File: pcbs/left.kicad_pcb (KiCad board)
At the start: 2 copper layers, 123.1 x 93.2 mm, 27 parts

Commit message: Remove top two mounting holes
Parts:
- removed H4, H5: , ceoloide:mounting_hole_plated
- moved H3 104.9 mm to (198.6, 101.6), turned to -26 degrees
- moved H1 68.4 mm to (94.4, 113.7)
- moved H2 67.2 mm to (135.1, 91.7)
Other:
- outline, holes or cut-outs redrawn
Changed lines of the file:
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@@
   (footprint "ceoloide:mounting_hole_plated"
     (layer "F.Cu")
-    (at 94.25093449999999 45.301295800000005 6)
+    (at 94.3972168 113.6604839 6)
     (property "Reference" "H1"
       (at 0 3 6)
@@
   (footprint "ceoloide:mounting_hole_plated"
     (layer "F.Cu")
-    (at 181.1483666 42.684291099999996 0)
+    (at 135.1483667 91.68429119999999 0)
     (property "Reference" "H2"
       (at 0 3 0)
@@
   (footprint "ceoloide:mounting_hole_plated"
     (layer "F.Cu")
-    (at 94.3972168 113.6604839 6)
+    (at 198.6292952 101.55924569999999 -26)
     (property "Reference" "H3"
-      (at 0 3 6)
-      (layer "F.SilkS")
-      hide
-      (effects (font (size 1 1) (thickness 0.15)))
-    )
-    (pad "" thru_hole circle (at 0 0 6) (size 3.8000000000000003 3.8000000000000003) (drill 2.2) (layers "*.Cu" "*.Mask"))
-    (fp_circle (center 0 0) (end -2.1500000000000004 0) (layer "F.CrtYd") (stroke (width 0.05) (type solid)) (fill none))
-    (fp_circle (center 0 0) (end -2.1500000000000004 0) (layer "B.CrtYd") (stroke (width 0.05) (type solid)) (fill none))
-  )
-  (footprint "ceoloide:mounting_hole_plated"
-    (layer "F.Cu")
-    (at 135.1483667 91.68429119999999 0)
-    (property "Reference" "H4"
-      (at 0 3 0)
-      (layer "F.SilkS")
-      hide
-      (effects (font (size 1 1) (thickness 0.15)))
-    )
-    (pad "" thru_hole circle (at 0 0 0) (size 3.8000000000000003 3.8000000000000003) (drill 2.2) (layers "*.Cu" "*.Mask"))
-    (fp_circle (center 0 0) (end -2.1500000000000004 0) (layer "F.CrtYd") (stroke (width 0.05) (type solid)) (fill none))
-    (fp_circle (center 0 0) (end -2.1500000000000004 0) (layer "B.CrtYd") (stroke (width 0.05) (type solid)) (fill none))
-  )
-  (footprint "ceoloide:mounting_hole_plated"
-    (layer "F.Cu")
-    (at 198.6292952 101.55924569999999 -26)
-    (property "Reference" "H5"
       (at 0 3 -26)
       (layer "F.SilkS")
@@
 (gr_line (start 143.1483666 95.68429119999999) (end 113.1483666 95.68429119999999) (layer Edge.Cuts) (stroke (width 0.15) (type default)))
 (gr_arc (start 113.1483666 95.68429119999999) (mid 112.4412598 95.97718439999998) (end 112.1483666 96.68429119999999) (layer Edge.Cuts) (stroke (width 0.15) (type default)))
-(gr_circle (center 94.25093449999999 45.301295800000005) (end 96.05093449999998 45.301295800000005) (layer Edge.Cuts) (stroke (width 0.15) (type default)) (fill none))
-(gr_circle (center 181.1483666 42.684291099999996) (end 182.9483666 42.684291099999996) (layer Edge.Cuts) (stroke (width 0.15) (type default)) (fill none))
 (gr_circle (center 135.1483667 91.68429119999999) (end 136.9483667 91.68429119999999) (layer Edge.Cuts) (stroke (width 0.15) (type default)) (fill none))
 (gr_circle (center 198.6292952 101.55924569999999) (end 200.4292952 101.55924569999999) (layer Edge.Cuts) (stroke (width 0.15) (type default)) (fill none))

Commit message: Remove bottom middle hole
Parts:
- removed H3: , ceoloide:mounting_hole_plated
- moved H2 64.2 mm to (198.6, 101.6), turned to -26 degrees
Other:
- outline, holes or cut-outs redrawn
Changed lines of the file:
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@@
-  (footprint "ceoloide:mounting_hole_plated"
-    (layer "F.Cu")
-    (at 135.1483667 91.68429119999999 0)
-    (property "Reference" "H2"
-      (at 0 3 0)
-      (layer "F.SilkS")
-      hide
-      (effects (font (size 1 1) (thickness 0.15)))
-    )
-    (pad "" thru_hole circle (at 0 0 0) (size 3.8000000000000003 3.8000000000000003) (drill 2.2) (layers "*.Cu" "*.Mask"))
-    (fp_circle (center 0 0) (end -2.1500000000000004 0) (layer "F.CrtYd") (stroke (width 0.05) (type solid)) (fill none))
-    (fp_circle (center 0 0) (end -2.1500000000000004 0) (layer "B.CrtYd") (stroke (width 0.05) (type solid)) (fill none))
-  )
   (footprint "ceoloide:mounting_hole_plated"
     (layer "F.Cu")
     (at 198.6292952 101.55924569999999 -26)
-    (property "Reference" "H3"
+    (property "Reference" "H2"
       (at 0 3 -26)
       (layer "F.SilkS")
@@
 (gr_line (start 143.1483666 95.68429119999999) (end 113.1483666 95.68429119999999) (layer Edge.Cuts) (stroke (width 0.15) (type default)))
 (gr_arc (start 113.1483666 95.68429119999999) (mid 112.4412598 95.97718439999998) (end 112.1483666 96.68429119999999) (layer Edge.Cuts) (stroke (width 0.15) (type default)))
-(gr_circle (center 135.1483667 91.68429119999999) (end 136.9483667 91.68429119999999) (layer Edge.Cuts) (stroke (width 0.15) (type default)) (fill none))
 (gr_circle (center 198.6292952 101.55924569999999) (end 200.4292952 101.55924569999999) (layer Edge.Cuts) (stroke (width 0.15) (type default)) (fill none))
 (gr_circle (center 94.3972168 113.6604839) (end 96.19721679999999 113.6604839) (layer Edge.Cuts) (stroke (width 0.15) (type default)) (fill none))

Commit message: Remove bottom right hole
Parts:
- removed H2: , ceoloide:mounting_hole_plated
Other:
- outline, holes or cut-outs redrawn
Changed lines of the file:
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@@
-    (fp_circle (center 0 0) (end -2.1500000000000004 0) (layer "B.CrtYd") (stroke (width 0.05) (type solid)) (fill none))
-  )
-  (footprint "ceoloide:mounting_hole_plated"
-    (layer "F.Cu")
-    (at 198.6292952 101.55924569999999 -26)
-    (property "Reference" "H2"
-      (at 0 3 -26)
-      (layer "F.SilkS")
-      hide
-      (effects (font (size 1 1) (thickness 0.15)))
-    )
-    (pad "" thru_hole circle (at 0 0 -26) (size 3.8000000000000003 3.8000000000000003) (drill 2.2) (layers "*.Cu" "*.Mask"))
-    (fp_circle (center 0 0) (end -2.1500000000000004 0) (layer "F.CrtYd") (stroke (width 0.05) (type solid)) (fill none))
     (fp_circle (center 0 0) (end -2.1500000000000004 0) (layer "B.CrtYd") (stroke (width 0.05) (type solid)) (fill none))
   )
@@
 (gr_line (start 143.1483666 95.68429119999999) (end 113.1483666 95.68429119999999) (layer Edge.Cuts) (stroke (width 0.15) (type default)))
 (gr_arc (start 113.1483666 95.68429119999999) (mid 112.4412598 95.97718439999998) (end 112.1483666 96.68429119999999) (layer Edge.Cuts) (stroke (width 0.15) (type default)))
-(gr_circle (center 198.6292952 101.55924569999999) (end 200.4292952 101.55924569999999) (layer Edge.Cuts) (stroke (width 0.15) (type default)) (fill none))
 (gr_circle (center 94.3972168 113.6604839) (end 96.19721679999999 113.6604839) (layer Edge.Cuts) (stroke (width 0.15) (type default)) (fill none))
 (gr_line (start 112.1483666 96.68429119999999) (end 112.1483666 116.68429119999999) (layer F.SilkS) (stroke (width 0.15) (type default)))

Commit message: Remove bottom left hole
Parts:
- removed H1: , ceoloide:mounting_hole_plated
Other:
- outline, holes or cut-outs redrawn
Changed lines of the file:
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@@
     )
-  )
-  (footprint "ceoloide:mounting_hole_plated"
-    (layer "F.Cu")
-    (at 94.3972168 113.6604839 6)
-    (property "Reference" "H1"
-      (at 0 3 6)
-      (layer "F.SilkS")
-      hide
-      (effects (font (size 1 1) (thickness 0.15)))
-    )
-    (pad "" thru_hole circle (at 0 0 6) (size 3.8000000000000003 3.8000000000000003) (drill 2.2) (layers "*.Cu" "*.Mask"))
-    (fp_circle (center 0 0) (end -2.1500000000000004 0) (layer "F.CrtYd") (stroke (width 0.05) (type solid)) (fill none))
-    (fp_circle (center 0 0) (end -2.1500000000000004 0) (layer "B.CrtYd") (stroke (width 0.05) (type solid)) (fill none))
   )
   (zone
@@
 (gr_line (start 143.1483666 95.68429119999999) (end 113.1483666 95.68429119999999) (layer Edge.Cuts) (stroke (width 0.15) (type default)))
 (gr_arc (start 113.1483666 95.68429119999999) (mid 112.4412598 95.97718439999998) (end 112.1483666 96.68429119999999) (layer Edge.Cuts) (stroke (width 0.15) (type default)))
-(gr_circle (center 94.3972168 113.6604839) (end 96.19721679999999 113.6604839) (layer Edge.Cuts) (stroke (width 0.15) (type default)) (fill none))
 (gr_line (start 112.1483666 96.68429119999999) (end 112.1483666 116.68429119999999) (layer F.SilkS) (stroke (width 0.15) (type default)))
 (gr_arc (start 112.1483666 116.68429119999999) (mid 112.4412598 117.391398) (end 113.1483666 117.68429119999999) (layer F.SilkS) (stroke (width 0.15) (type default)))

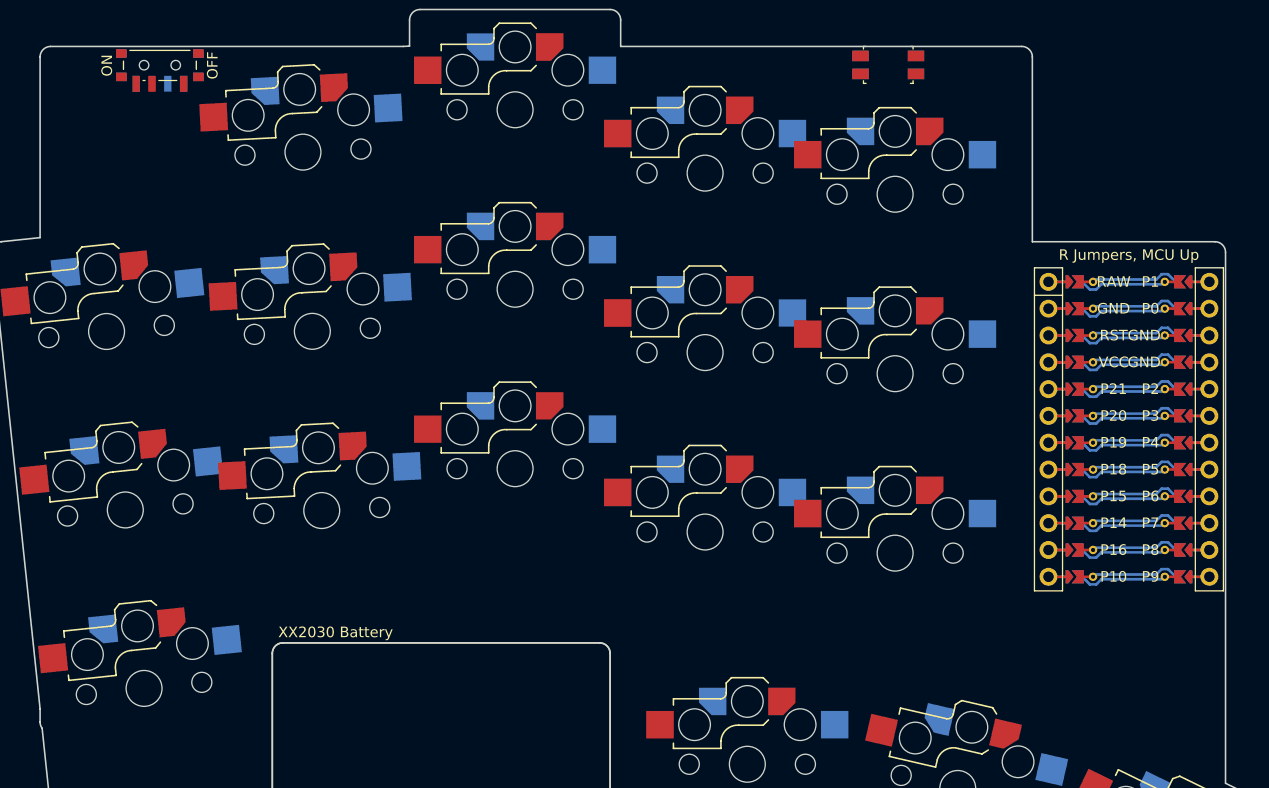
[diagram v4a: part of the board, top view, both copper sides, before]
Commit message: Restore holes except bottom left
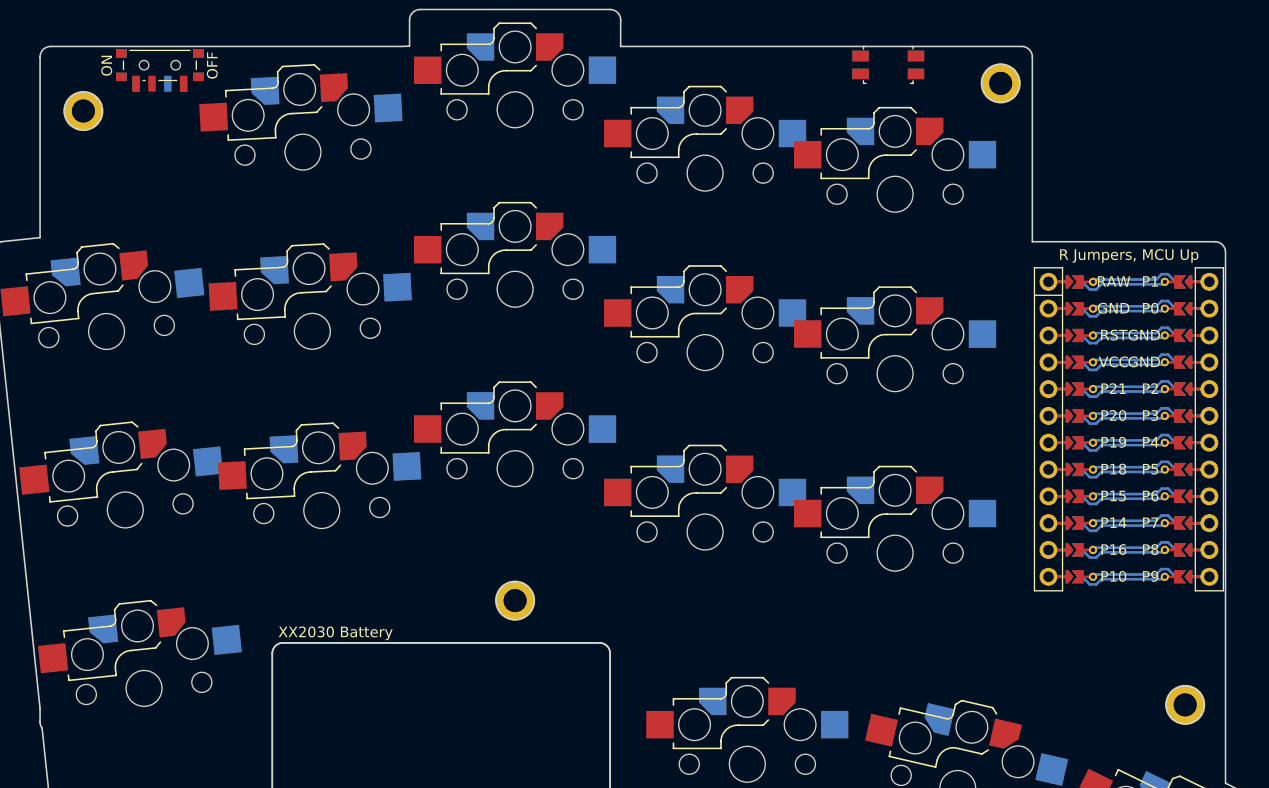
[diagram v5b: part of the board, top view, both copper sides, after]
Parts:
- added H1: , ceoloide:mounting_hole_plated, F.Cu at (94.3, 45.3)
- added H2: , ceoloide:mounting_hole_plated, F.Cu at (181.1, 42.7)
- added H3: , ceoloide:mounting_hole_plated, F.Cu at (135.1, 91.7)
- added H4: , ceoloide:mounting_hole_plated, F.Cu at (198.6, 101.6)
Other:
- outline, holes or cut-outs redrawn
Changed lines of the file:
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@@
     )
+  )
+  (footprint "ceoloide:mounting_hole_plated"
+    (layer "F.Cu")
+    (at 94.25093449999999 45.301295800000005 6)
+    (property "Reference" "H1"
+      (at 0 3 6)
+      (layer "F.SilkS")
+      hide
+      (effects (font (size 1 1) (thickness 0.15)))
+    )
+    (pad "" thru_hole circle (at 0 0 6) (size 3.8000000000000003 3.8000000000000003) (drill 2.2) (layers "*.Cu" "*.Mask"))
+    (fp_circle (center 0 0) (end -2.1500000000000004 0) (layer "F.CrtYd") (stroke (width 0.05) (type solid)) (fill none))
+    (fp_circle (center 0 0) (end -2.1500000000000004 0) (layer "B.CrtYd") (stroke (width 0.05) (type solid)) (fill none))
+  )
+  (footprint "ceoloide:mounting_hole_plated"
+    (layer "F.Cu")
+    (at 181.1483666 42.684291099999996 0)
+    (property "Reference" "H2"
+      (at 0 3 0)
+      (layer "F.SilkS")
+      hide
+      (effects (font (size 1 1) (thickness 0.15)))
+    )
+    (pad "" thru_hole circle (at 0 0 0) (size 3.8000000000000003 3.8000000000000003) (drill 2.2) (layers "*.Cu" "*.Mask"))
+    (fp_circle (center 0 0) (end -2.1500000000000004 0) (layer "F.CrtYd") (stroke (width 0.05) (type solid)) (fill none))
+    (fp_circle (center 0 0) (end -2.1500000000000004 0) (layer "B.CrtYd") (stroke (width 0.05) (type solid)) (fill none))
+  )
+  (footprint "ceoloide:mounting_hole_plated"
+    (layer "F.Cu")
+    (at 135.1483667 91.68429119999999 0)
+    (property "Reference" "H3"
+      (at 0 3 0)
+      (layer "F.SilkS")
+      hide
+      (effects (font (size 1 1) (thickness 0.15)))
+    )
+    (pad "" thru_hole circle (at 0 0 0) (size 3.8000000000000003 3.8000000000000003) (drill 2.2) (layers "*.Cu" "*.Mask"))
+    (fp_circle (center 0 0) (end -2.1500000000000004 0) (layer "F.CrtYd") (stroke (width 0.05) (type solid)) (fill none))
+    (fp_circle (center 0 0) (end -2.1500000000000004 0) (layer "B.CrtYd") (stroke (width 0.05) (type solid)) (fill none))
+  )
+  (footprint "ceoloide:mounting_hole_plated"
+    (layer "F.Cu")
+    (at 198.6292952 101.55924569999999 -26)
+    (property "Reference" "H4"
+      (at 0 3 -26)
+      (layer "F.SilkS")
+      hide
+      (effects (font (size 1 1) (thickness 0.15)))
+    )
+    (pad "" thru_hole circle (at 0 0 -26) (size 3.8000000000000003 3.8000000000000003) (drill 2.2) (layers "*.Cu" "*.Mask"))
+    (fp_circle (center 0 0) (end -2.1500000000000004 0) (layer "F.CrtYd") (stroke (width 0.05) (type solid)) (fill none))
+    (fp_circle (center 0 0) (end -2.1500000000000004 0) (layer "B.CrtYd") (stroke (width 0.05) (type solid)) (fill none))
   )
   (zone
@@
 (gr_line (start 143.1483666 95.68429119999999) (end 113.1483666 95.68429119999999) (layer Edge.Cuts) (stroke (width 0.15) (type default)))
 (gr_arc (start 113.1483666 95.68429119999999) (mid 112.4412598 95.97718439999998) (end 112.1483666 96.68429119999999) (layer Edge.Cuts) (stroke (width 0.15) (type default)))
+(gr_circle (center 94.25093449999999 45.301295800000005) (end 96.05093449999998 45.301295800000005) (layer Edge.Cuts) (stroke (width 0.15) (type default)) (fill none))
+(gr_circle (center 181.1483666 42.684291099999996) (end 182.9483666 42.684291099999996) (layer Edge.Cuts) (stroke (width 0.15) (type default)) (fill none))
+(gr_circle (center 135.1483667 91.68429119999999) (end 136.9483667 91.68429119999999) (layer Edge.Cuts) (stroke (width 0.15) (type default)) (fill none))
+(gr_circle (center 198.6292952 101.55924569999999) (end 200.4292952 101.55924569999999) (layer Edge.Cuts) (stroke (width 0.15) (type default)) (fill none))
 (gr_line (start 112.1483666 96.68429119999999) (end 112.1483666 116.68429119999999) (layer F.SilkS) (stroke (width 0.15) (type default)))
 (gr_arc (start 112.1483666 116.68429119999999) (mid 112.4412598 117.391398) (end 113.1483666 117.68429119999999) (layer F.SilkS) (stroke (width 0.15) (type default)))

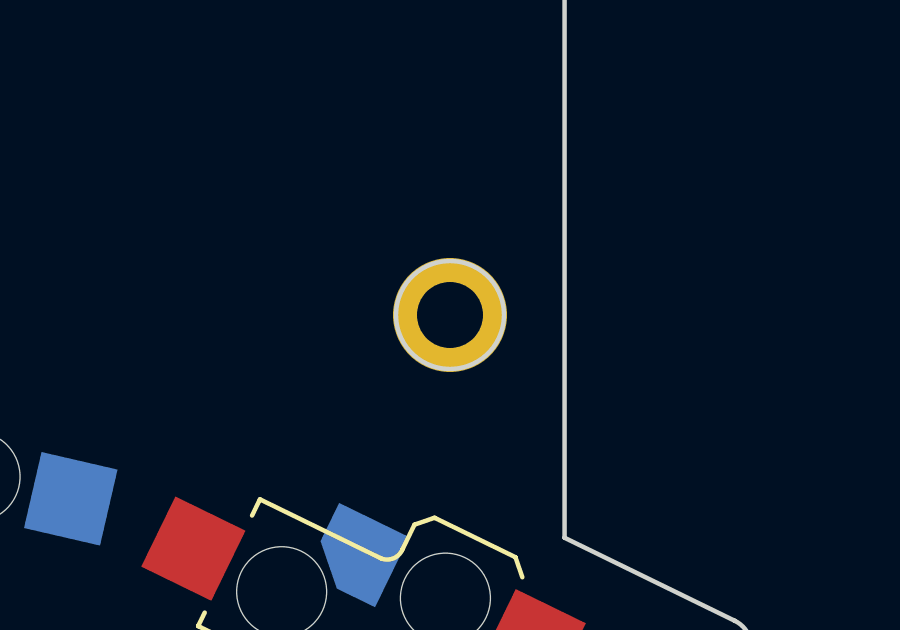
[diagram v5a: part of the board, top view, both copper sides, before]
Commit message: Remove bottom right hole
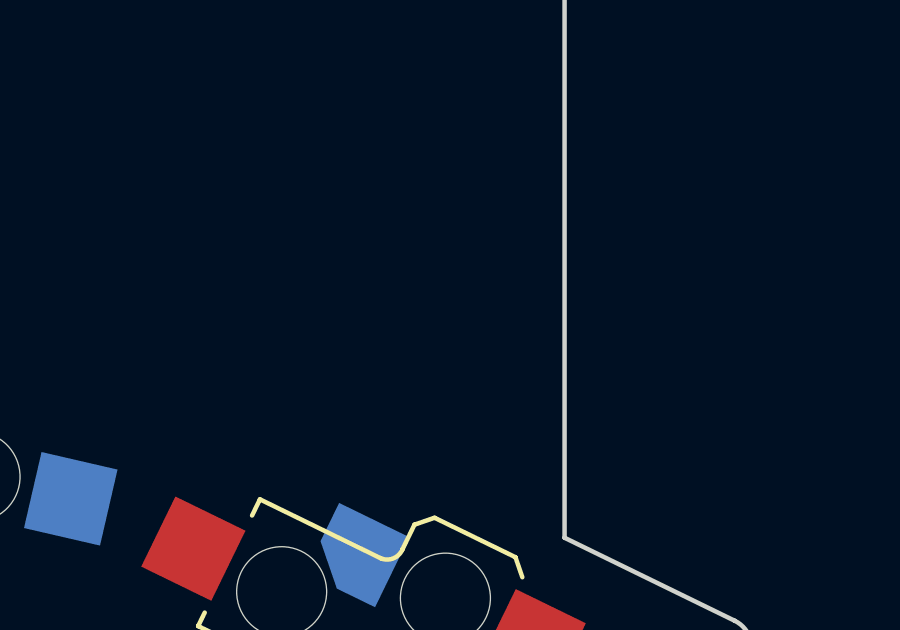
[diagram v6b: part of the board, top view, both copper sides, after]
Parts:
- removed H4: , ceoloide:mounting_hole_plated
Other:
- outline, holes or cut-outs redrawn
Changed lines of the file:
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@@
-    (fp_circle (center 0 0) (end -2.1500000000000004 0) (layer "B.CrtYd") (stroke (width 0.05) (type solid)) (fill none))
-  )
-  (footprint "ceoloide:mounting_hole_plated"
-    (layer "F.Cu")
-    (at 198.6292952 101.55924569999999 -26)
-    (property "Reference" "H4"
-      (at 0 3 -26)
-      (layer "F.SilkS")
-      hide
-      (effects (font (size 1 1) (thickness 0.15)))
-    )
-    (pad "" thru_hole circle (at 0 0 -26) (size 3.8000000000000003 3.8000000000000003) (drill 2.2) (layers "*.Cu" "*.Mask"))
-    (fp_circle (center 0 0) (end -2.1500000000000004 0) (layer "F.CrtYd") (stroke (width 0.05) (type solid)) (fill none))
     (fp_circle (center 0 0) (end -2.1500000000000004 0) (layer "B.CrtYd") (stroke (width 0.05) (type solid)) (fill none))
   )
@@
 (gr_circle (center 181.1483666 42.684291099999996) (end 182.9483666 42.684291099999996) (layer Edge.Cuts) (stroke (width 0.15) (type default)) (fill none))
 (gr_circle (center 135.1483667 91.68429119999999) (end 136.9483667 91.68429119999999) (layer Edge.Cuts) (stroke (width 0.15) (type default)) (fill none))
-(gr_circle (center 198.6292952 101.55924569999999) (end 200.4292952 101.55924569999999) (layer Edge.Cuts) (stroke (width 0.15) (type default)) (fill none))
 (gr_line (start 112.1483666 96.68429119999999) (end 112.1483666 116.68429119999999) (layer F.SilkS) (stroke (width 0.15) (type default)))
 (gr_arc (start 112.1483666 116.68429119999999) (mid 112.4412598 117.391398) (end 113.1483666 117.68429119999999) (layer F.SilkS) (stroke (width 0.15) (type default)))
